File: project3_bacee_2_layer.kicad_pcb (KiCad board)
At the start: 2 copper layers, 41.9 x 29 mm, 17 parts, among them J1 Digital Pins, J2 Serial, J3 ICSP, J4 I2C, U1 24LC1025, U2 24LC1025, U3 DS13375+, U4 ATMEGA328P-AU, Y1 Crystal 32Mhz, Y2 Crystal 16Mhz

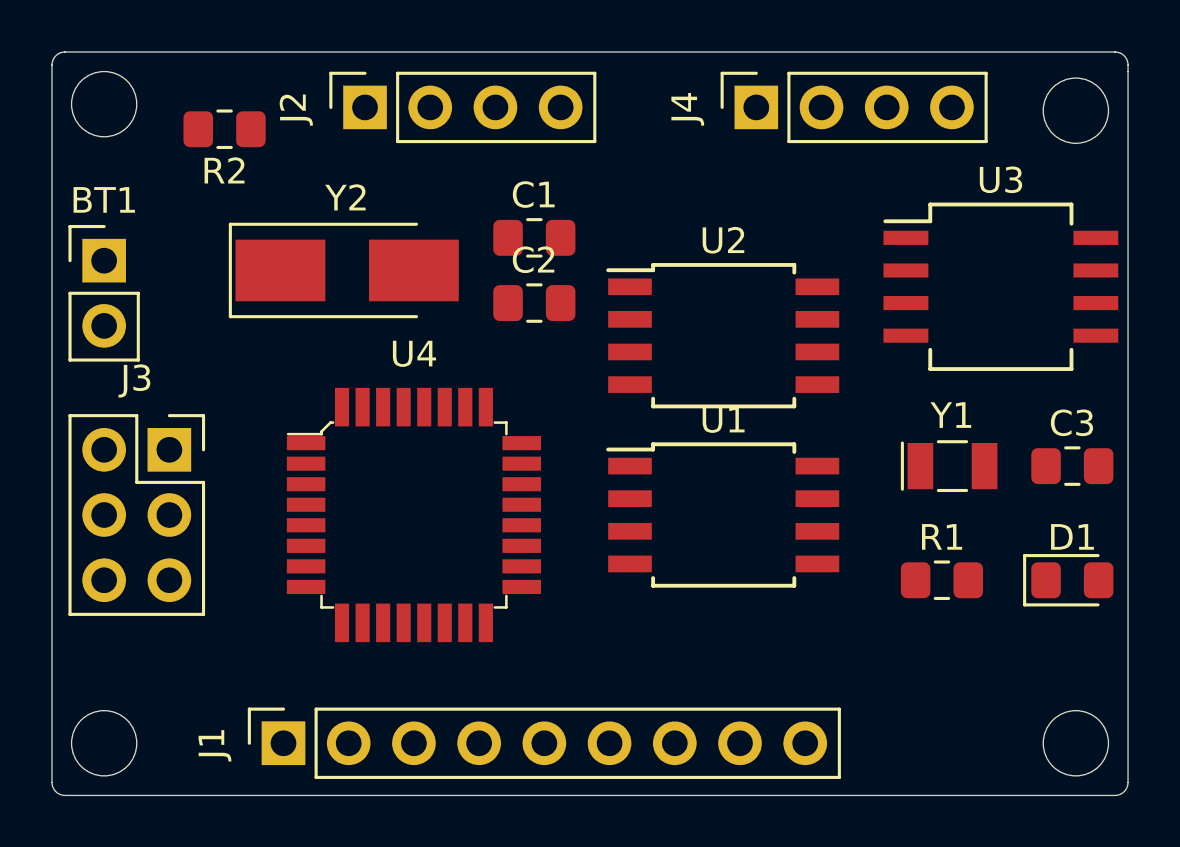
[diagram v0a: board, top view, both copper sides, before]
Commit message: 2 layer autorouted
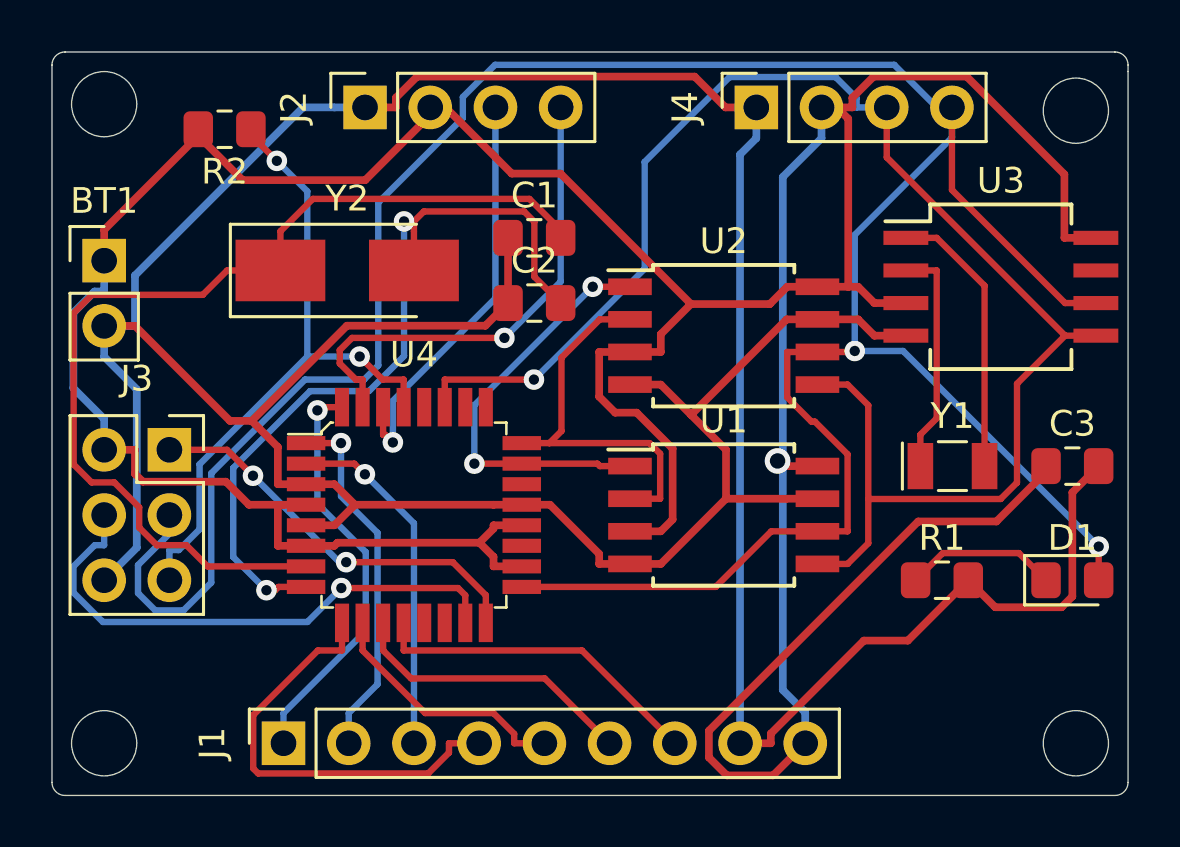
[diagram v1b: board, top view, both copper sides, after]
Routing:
- net /Vcc: track 0.00 -> 159.9 mm, vias 0 -> 1
- net GNDPWR: track 0.00 -> 156.5 mm
- net /SCK: track 0.00 -> 111.9 mm, vias 0 -> 2
- net /SDA: track 0.00 -> 61.8 mm, vias 0 -> 1
- net Net-(C1-Pad2): track 0.00 -> 39.6 mm
- net Net-(C2-Pad2): track 0.00 -> 31.5 mm, vias 0 -> 2
- net /RESET: track 0.00 -> 26.1 mm, vias 0 -> 2
- net /MOSI: track 0.00 -> 21.2 mm, vias 0 -> 1
- net /Tx: track 0.00 -> 19.2 mm, vias 0 -> 1
- net /D5: track 0.00 -> 17.2 mm
- net /ADDS1: track 0.00 -> 16.4 mm, vias 0 -> 2
- net /Rx: track 0.00 -> 16.3 mm, vias 0 -> 1
- net /D2: track 0.00 -> 16.1 mm, vias 0 -> 1
- net /MISO: track 0.00 -> 15.7 mm, vias 0 -> 2
- net /ADDS2: track 0.00 -> 15.3 mm
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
